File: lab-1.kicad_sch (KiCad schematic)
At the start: 25 parts, among them J1 Conn_01x04_Pin, J2 USB_C_Receptacle, U1 LM66100DCK, U2 LM66100DCK, U3 STM32F405RGTx, U4 MCP1700x-120xxMB, Y1 8 MHz

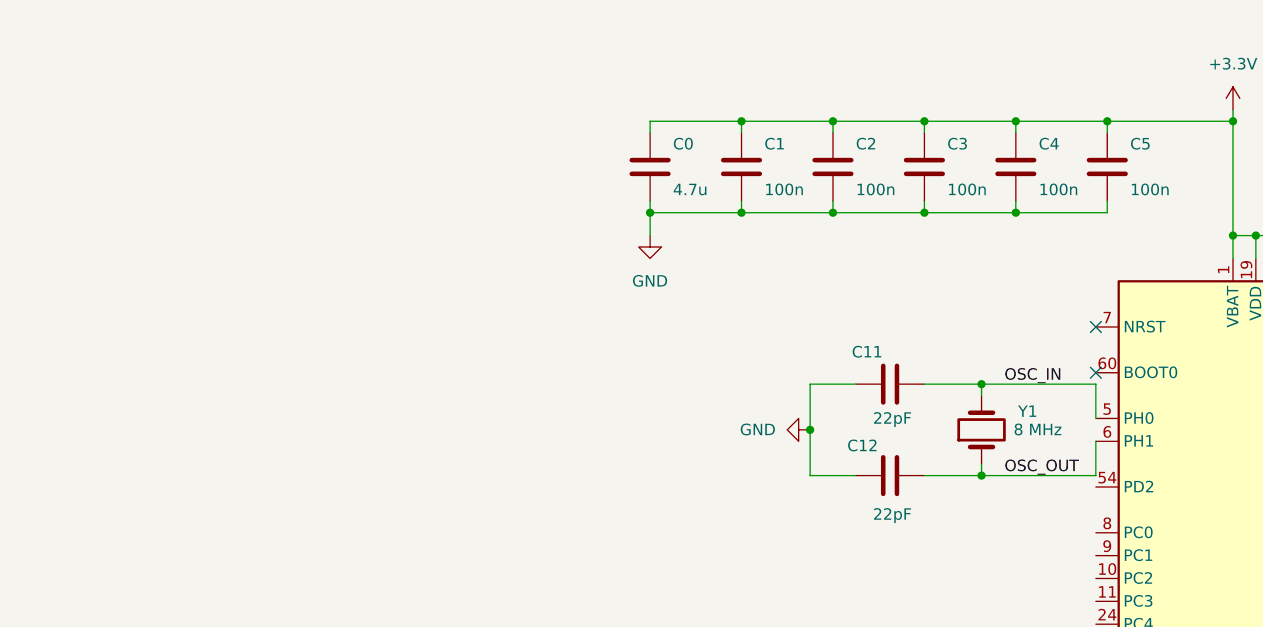
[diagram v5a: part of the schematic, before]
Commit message: Added buttons
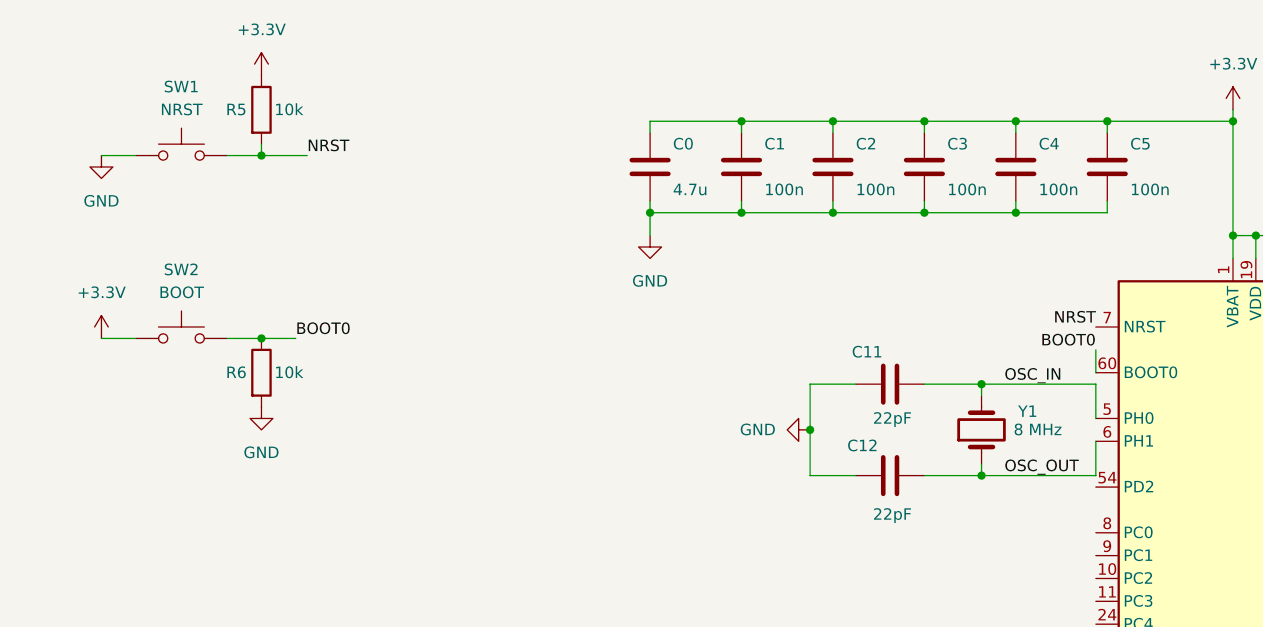
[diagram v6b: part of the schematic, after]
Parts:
- added R5, R6: 10k, Resistor_SMD:R_0402_1005Metric, symbol Device:R
- added SW1: NRST, Button_Switch_THT:SW_PUSH_6mm_H4.3mm, symbol Switch:SW_Push
- added SW2: BOOT, Button_Switch_THT:SW_PUSH_6mm_H4.3mm, symbol Switch:SW_Push
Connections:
- net +3.3V: now also R5.1, SW2.2
- net GND: now also R6.2, SW1.2
- net BOOT0: now reaches U3.60 (BOOT0)
- net BOOT0: now also R6.1, SW2.1
- net NRST: now reaches U3.7 (NRST)
- net NRST: now also R5.2, SW1.1
- no-connect marks 2 -> 0

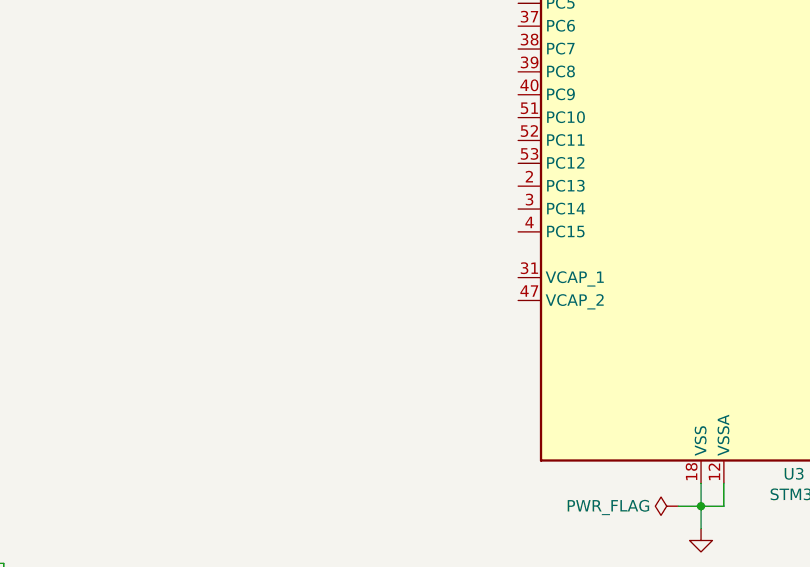
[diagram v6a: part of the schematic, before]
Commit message: add VCAP
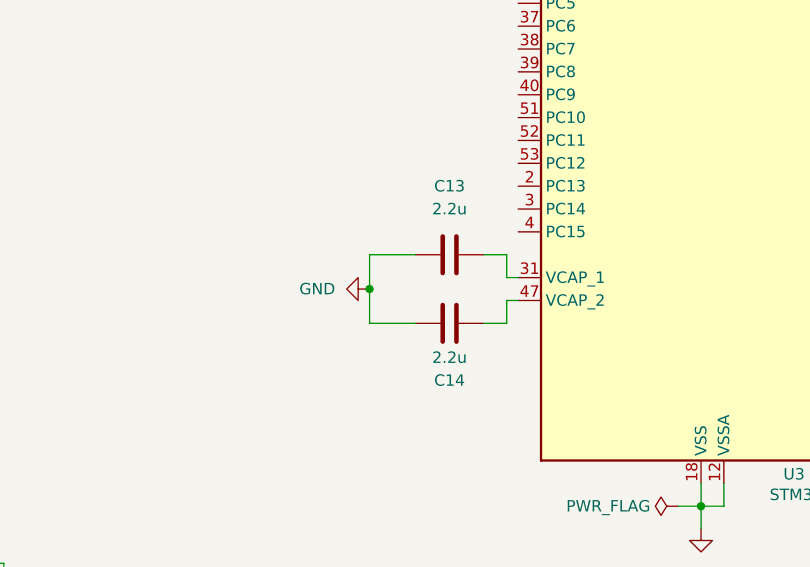
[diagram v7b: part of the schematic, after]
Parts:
- added C13, C14: 2.2u, Capacitor_SMD:C_0402_1005Metric, symbol Device:C
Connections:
- net GND: now also C13.1, C14.2
- net at U3.31 (VCAP_1): now also C13.2
- net at U3.47 (VCAP_2): now also C14.1

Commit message: minor adjustments
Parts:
- removed R4: 100k, Resistor_SMD:R_0603_1608Metric, symbol Device:R
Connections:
- net +3.3V: now also U1.3 (~{CE})
- net +3.3V_LDO: now also R3.2, U2.3 (~{CE}); no longer R3.1
- net +3.3V_STLINK: no longer U1.3 (~{CE})
- net GND: now also R3.1, U1.5 (ST)
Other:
- moved on the sheet: J1, R1, R2, R3, R5, R6, SW1, SW2
